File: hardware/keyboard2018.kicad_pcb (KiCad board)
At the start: 2 copper layers, 339.1 x 116.8 mm, 190 parts, among them J1 USB_B_no_shield, J2 Conn_01x05_Male, SW1 SW_Push, U1 PIC16F1454-IP, U2 PIC16F18855-IP

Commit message: Adjust some mechanical stuff
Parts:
- moved REF** 2.54 mm to (177.8, 194.9)

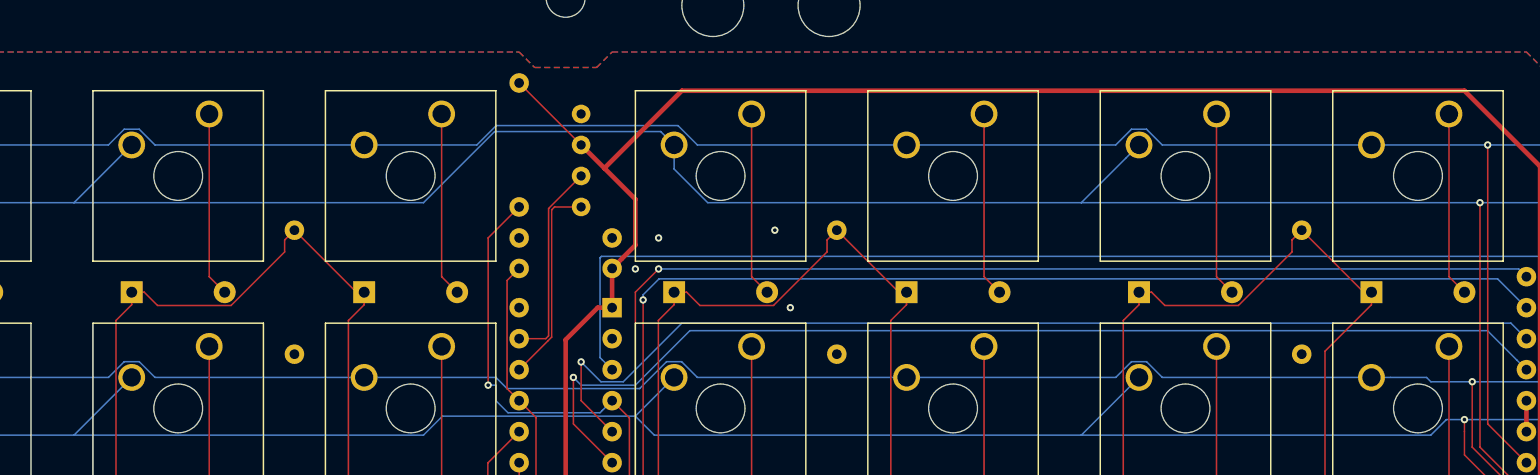
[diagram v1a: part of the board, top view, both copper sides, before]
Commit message: Nudge a couple footprints
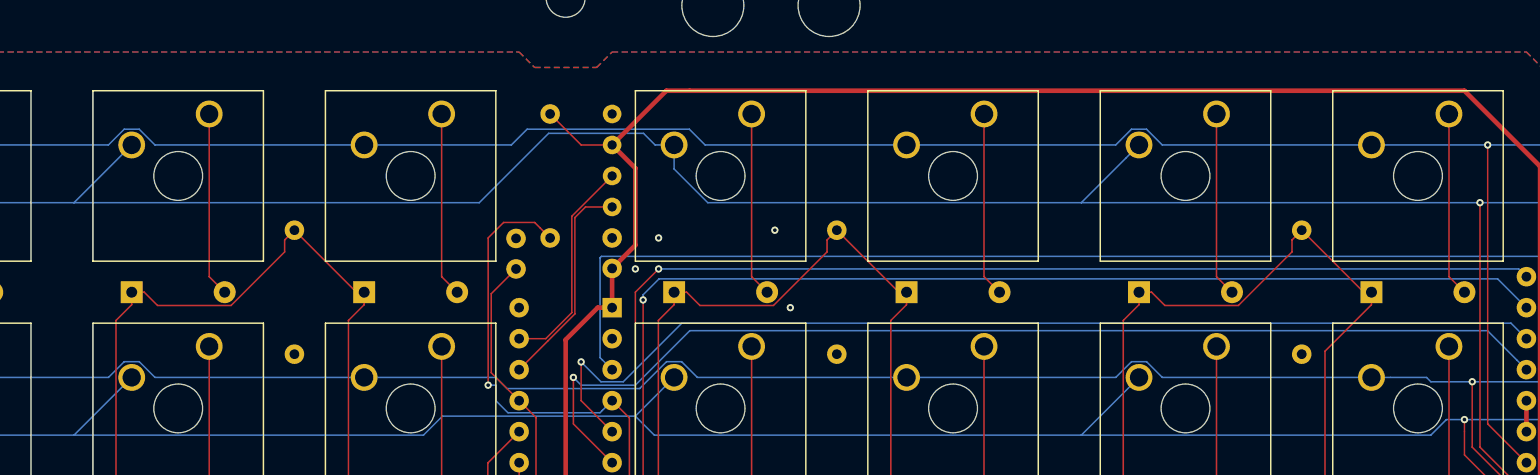
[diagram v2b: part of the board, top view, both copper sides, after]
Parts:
- moved R9 3.59 mm to (176.5, 96.5)
- moved J1 2.54 mm to (181.6, 100.3)
- moved C2 0.26 mm to (173.7, 106.7)
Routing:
- net VDD: track 179.2 -> 175.7 mm
- net /~MCLR~_EXT: track 67.4 -> 70.0 mm
- net /D+: track 16.7 -> 17.8 mm
- net /D-: track 16.7 -> 17.8 mm
- net Net-(C2-Pad2): track 24.6 -> 25.5 mm

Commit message: Adjust holes, cuts, and edges
Hopefully this is right.
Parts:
- moved REF** 2.54 mm to (177.8, 192.4)
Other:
- board size 339.1 x 116.8 mm -> 342.9 x 120.7 mm
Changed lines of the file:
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@@
   (general
     (thickness 1.6)
-    (drawings 30)
+    (drawings 70)
     (tracks 1076)
     (zones 0)
@@
   (page User 431.8 279.4)
   (layers
-    (0 F.Cu signal)
-    (31 B.Cu signal)
+    (0 F.Cu signal hide)
+    (31 B.Cu signal hide)
     (33 F.Adhes user hide)
     (36 B.SilkS user)
@@
   )
   (module custom:M3_hole (layer F.Cu)
-    (at 177.8 194.945)
+    (at 177.8 192.405)
     (descr "Mounting Hole 3.2mm, no annular, M3")
     (tags "mounting hole 3.2mm no annular m3")
@@
     )
   )
+  (gr_line (start 186.055 79.248) (end 203.2 79.248) (layer Eco1.User) (width 0.0508))
+  (gr_line (start 203.2 79.248) (end 382.905 79.248) (layer Eco1.User) (width 0.0508))
+  (gr_line (start 203.2 90.17) (end 372.11 90.17) (layer Eco1.User) (width 0.0508))
+  (gr_line (start 186.055 90.17) (end 203.2 90.17) (layer Eco1.User) (width 0.0508))
+  (gr_arc (start 203.2 81.153) (end 203.2 79.248) (angle -90) (layer Eco1.User) (width 0.0508))
+  (gr_arc (start 186.055 81.153) (end 187.96 81.153) (angle -90) (layer Eco1.User) (width 0.0508))
+  (gr_line (start 187.96 88.265) (end 187.96 81.153) (layer Eco1.User) (width 0.0508))
+  (gr_line (start 201.295 88.265) (end 201.295 81.153) (layer Eco1.User) (width 0.0508))
+  (gr_arc (start 203.2 88.265) (end 201.295 88.265) (angle -90) (layer Eco1.User) (width 0.0508))
+  (gr_arc (start 186.055 88.265) (end 186.055 90.17) (angle -90) (layer Eco1.User) (width 0.0508))
+  (gr_line (start 266.7 92.71) (end 266.7 92.075) (layer Eco1.User) (width 0.0508))
+  (gr_line (start 255.905 94.615) (end 264.795 94.615) (layer Eco1.User) (width 0.0508))
+  (gr_line (start 254 92.075) (end 254 92.71) (layer Eco1.User) (width 0.0508))
+  (gr_line (start 184.15 92.075) (end 184.15 92.71) (layer Eco1.User) (width 0.0508))
+  (gr_line (start 173.355 94.615) (end 182.245 94.615) (layer Eco1.User) (width 0.0508))
+  (gr_line (start 171.45 92.075) (end 171.45 92.71) (layer Eco1.User) (width 0.0508))
+  (gr_line (start 171.45 186.69) (end 171.45 187.325) (layer Eco1.User) (width 0.0508))
+  (gr_line (start 182.245 184.785) (end 173.355 184.785) (layer Eco1.User) (width 0.0508))
+  (gr_line (start 184.15 186.69) (end 184.15 187.325) (layer Eco1.User) (width 0.0508))
+  (gr_line (start 266.7 186.69) (end 266.7 187.325) (layer Eco1.User) (width 0.0508))
+  (gr_line (start 255.905 184.785) (end 264.795 184.785) (layer Eco1.User) (width 0.0508))
+  (gr_line (start 254 186.69) (end 254 187.325) (layer Eco1.User) (width 0.0508))
+  (gr_arc (start 264.795 186.69) (end 266.7 186.69) (angle -90) (layer Eco1.User) (width 0.0508))
+  (gr_arc (start 252.095 187.325) (end 252.095 189.23) (angle -90) (layer Eco1.User) (width 0.0508))
+  (gr_arc (start 268.605 187.325) (end 266.7 187.325) (angle -90) (layer Eco1.User) (width 0.0508))
+  (gr_arc (start 255.905 186.69) (end 255.905 184.785) (angle -90) (layer Eco1.User) (width 0.0508))
+  (gr_arc (start 186.055 187.325) (end 184.15 187.325) (angle -90) (layer Eco1.User) (width 0.0508))
+  (gr_arc (start 182.245 186.69) (end 184.15 186.69) (angle -90) (layer Eco1.User) (width 0.0508))
+  (gr_arc (start 173.355 186.69) (end 173.355 184.785) (angle -90) (layer Eco1.User) (width 0.0508))
+  (gr_arc (start 169.545 187.325) (end 169.545 189.23) (angle -90) (layer Eco1.User) (width 0.0508))
+  (gr_arc (start 252.095 92.075) (end 254 92.075) (angle -90) (layer Eco1.User) (width 0.0508))
+  (gr_arc (start 255.905 92.71) (end 254 92.71) (angle -90) (layer Eco1.User) (width 0.0508))
+  (gr_arc (start 264.795 92.71) (end 264.795 94.615) (angle -90) (layer Eco1.User) (width 0.0508))
+  (gr_arc (start 268.605 92.075) (end 268.605 90.17) (angle -90) (layer Eco1.User) (width 0.0508))
+  (gr_arc (start 186.055 92.075) (end 186.055 90.17) (angle -90) (layer Eco1.User) (width 0.0508))
+  (gr_arc (start 182.245 92.71) (end 182.245 94.615) (angle -90) (layer Eco1.User) (width 0.0508))
+  (gr_arc (start 173.355 92.71) (end 171.45 92.71) (angle -90) (layer Eco1.User) (width 0.0508))
+  (gr_arc (start 169.545 92.075) (end 171.45 92.075) (angle -90) (layer Eco1.User) (width 0.0508))
+  (gr_arc (start 382.905 86.995) (end 390.652 86.995) (angle -90) (layer Eco1.User) (width 0.0508))
+  (gr_arc (start 382.905 192.405) (end 382.905 200.152) (angle -90) (layer Eco1.User) (width 0.0508))
+  (gr_arc (start 55.245 192.405) (end 47.498 192.405) (angle -90) (layer Eco1.User) (width 0.0508))
+  (gr_arc (start 55.245 86.995) (end 55.245 79.248) (angle -90) (layer Eco1.User) (width 0.0508))
+  (gr_arc (start 55.245 86.995) (end 55.245 79.375) (angle -90) (layer Edge.Cuts) (width 0.0508))
+  (gr_arc (start 55.245 192.405) (end 47.625 192.405) (angle -90) (layer Edge.Cuts) (width 0.0508))
+  (gr_arc (start 382.905 192.405) (end 382.905 200.025) (angle -90) (layer Edge.Cuts) (width 0.0508))
+  (gr_arc (start 382.905 86.995) (end 390.525 86.995) (angle -90) (layer Edge.Cuts) (width 0.0508))
   (gr_line (start 58.42 181.61) (end 58.42 97.79) (layer Eco1.User) (width 0.0508))
   (gr_line (start 372.11 189.23) (end 66.04 189.23) (layer Eco1.User) (width 0.0508))
   (gr_line (start 379.73 97.79) (end 379.73 181.61) (layer Eco1.User) (width 0.0508))
-  (gr_line (start 66.04 90.17) (end 372.11 90.17) (layer Eco1.User) (width 0.0508))
+  (gr_line (start 66.04 90.17) (end 169.545 90.17) (layer Eco1.User) (width 0.0508))
   (gr_arc (start 66.04 97.79) (end 66.04 90.17) (angle -90) (layer Eco1.User) (width 0.0508))
   (gr_arc (start 372.11 97.79) (end 379.73 97.79) (angle -90) (layer Eco1.User) (width 0.0508))
   (gr_arc (start 372.11 181.61) (end 372.11 189.23) (angle -90) (layer Eco1.User) (width 0.0508))
   (gr_arc (start 66.04 181.61) (end 58.42 181.61) (angle -90) (layer Eco1.User) (width 0.0508))
-  (gr_line (start 208.407 81.153) (end 384.81 81.153) (layer Eco1.User) (width 0.0508))
-  (gr_line (start 180.848 81.153) (end 208.407 81.153) (layer Eco1.User) (width 0.0508))
-  (gr_arc (start 53.34 194.31) (end 49.53 194.31) (angle -90) (layer Edge.Cuts) (width 0.0508))
-  (gr_arc (start 53.34 85.09) (end 53.34 81.28) (angle -90) (layer Edge.Cuts) (width 0.0508))
-  (gr_arc (start 53.34 194.31) (end 49.403 194.31) (angle -90) (layer Eco1.User) (width 0.0508))
-  (gr_arc (start 53.34 85.09) (end 53.34 81.153) (angle -90) (layer Eco1.User) (width 0.0508))
-  (gr_line (start 49.403 194.31) (end 49.403 85.09) (layer Eco1.User) (width 0.0508))
-  (gr_line (start 384.81 198.247) (end 53.34 198.247) (layer Eco1.User) (width 0.0508))
-  (gr_line (start 388.747 85.09) (end 388.747 194.31) (layer Eco1.User) (width 0.0508))
-  (gr_line (start 53.34 81.153) (end 180.848 81.153) (layer Eco1.User) (width 0.0508))
-  (gr_line (start 384.81 81.28) (end 53.34 81.28) (layer Edge.Cuts) (width 0.0508))
-  (gr_line (start 388.62 194.31) (end 388.62 85.09) (layer Edge.Cuts) (width 0.0508))
-  (gr_line (start 53.34 198.12) (end 384.81 198.12) (layer Edge.Cuts) (width 0.0508))
-  (gr_line (start 49.53 85.09) (end 49.53 194.31) (layer Edge.Cuts) (width 0.0508))
+  (gr_line (start 55.245 79.248) (end 186.055 79.248) (layer Eco1.User) (width 0.0508))
+  (gr_line (start 47.498 192.405) (end 47.498 86.995) (layer Eco1.User) (width 0.0508))
+  (gr_line (start 382.905 200.152) (end 55.245 200.152) (layer Eco1.User) (width 0.0508))
+  (gr_line (start 390.652 86.995) (end 390.652 192.405) (layer Eco1.User) (width 0.0508))
+  (gr_line (start 382.905 79.375) (end 55.245 79.375) (layer Edge.Cuts) (width 0.0508))
+  (gr_line (start 390.525 192.405) (end 390.525 86.995) (layer Edge.Cuts) (width 0.0508))
+  (gr_line (start 55.245 200.025) (end 382.905 200.025) (layer Edge.Cuts) (width 0.0508))
+  (gr_line (start 47.625 86.995) (end 47.625 192.405) (layer Edge.Cuts) (width 0.0508))
   (gr_text "blue lines: cut" (at 312.42 237.49) (layer Eco1.User)
     (effects (font (size 1.5 1.5) (thickness 0.3)) (justify left))

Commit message: I think it's done!
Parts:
- SW_A6, SW_B6, SW_C6, SW_D6, SW_E6: value SWA6 -> SW_Push
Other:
- board text added: "kbie"
- board text added: "kbie MKF"
- board text removed: "Maia keyboard 2018"
